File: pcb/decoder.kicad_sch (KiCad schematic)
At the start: 77 parts, among them J1 Conn_01x03_Socket, J2 Conn_01x03_Socket, J3 Conn_01x02_Socket, J4 Conn_01x02_Socket, J5 Conn_01x02_Socket, J6 Conn_01x02_Socket, J7 Conn_01x02_Socket, J8 Conn_01x03_Socket, Q1 IRLZ44N, Q10 BC817, Q11 FQP27P06, Q12 BC817, Q13 FQP27P06, Q15 BC817, Q2 FQP27P06, Q3 FQP27P06, Q4 IRLZ44N, Q5 BC817, Q6 BC817, Q7 FQP27P06, Q8 BC817, Q9 FQP27P06, U1 LM7805, U3 6N137

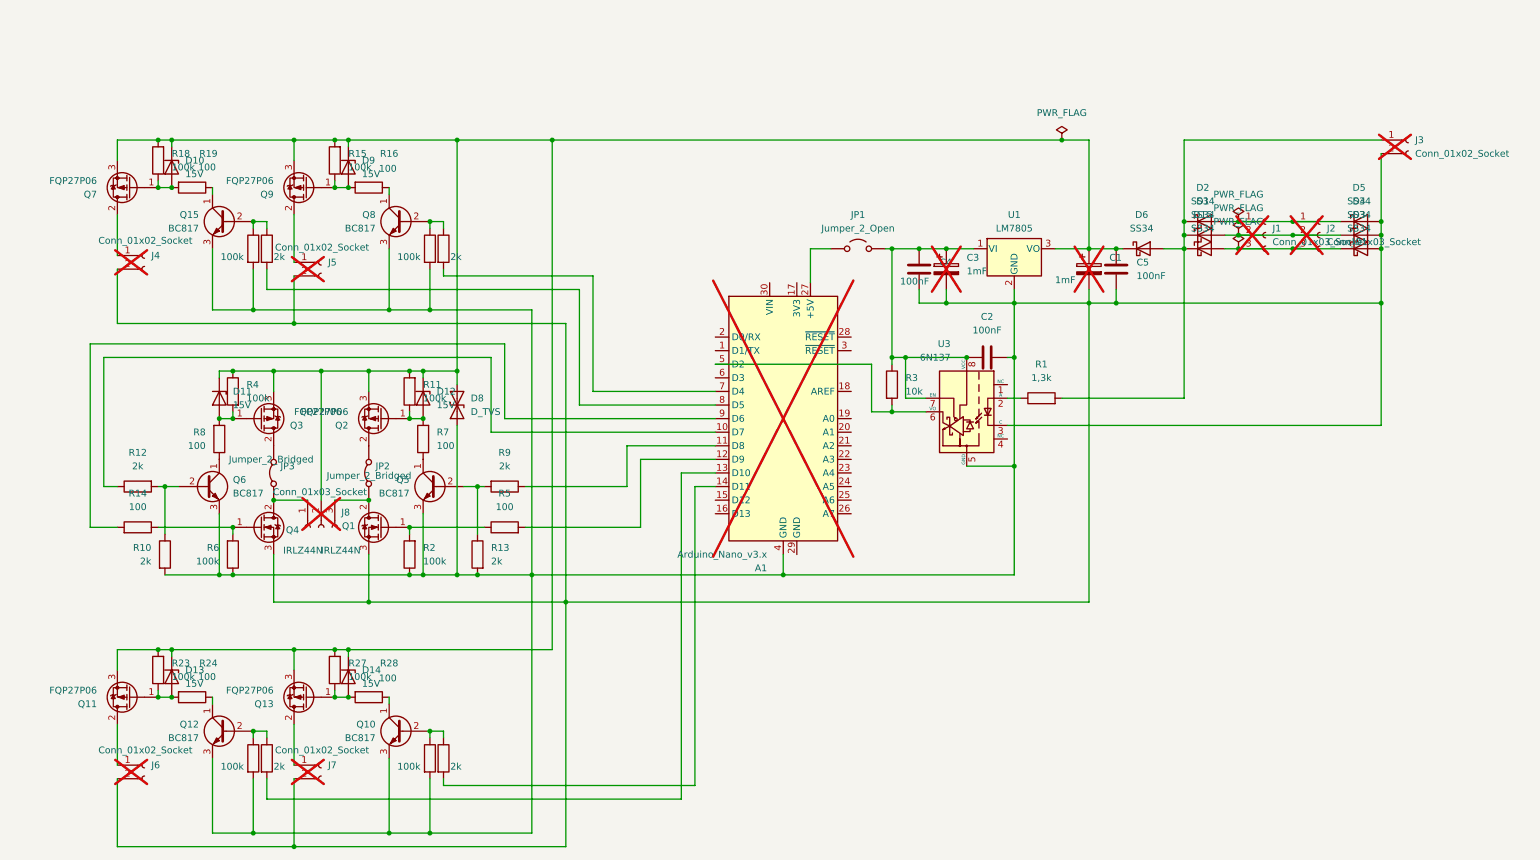
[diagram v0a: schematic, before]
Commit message: make PCB smaller
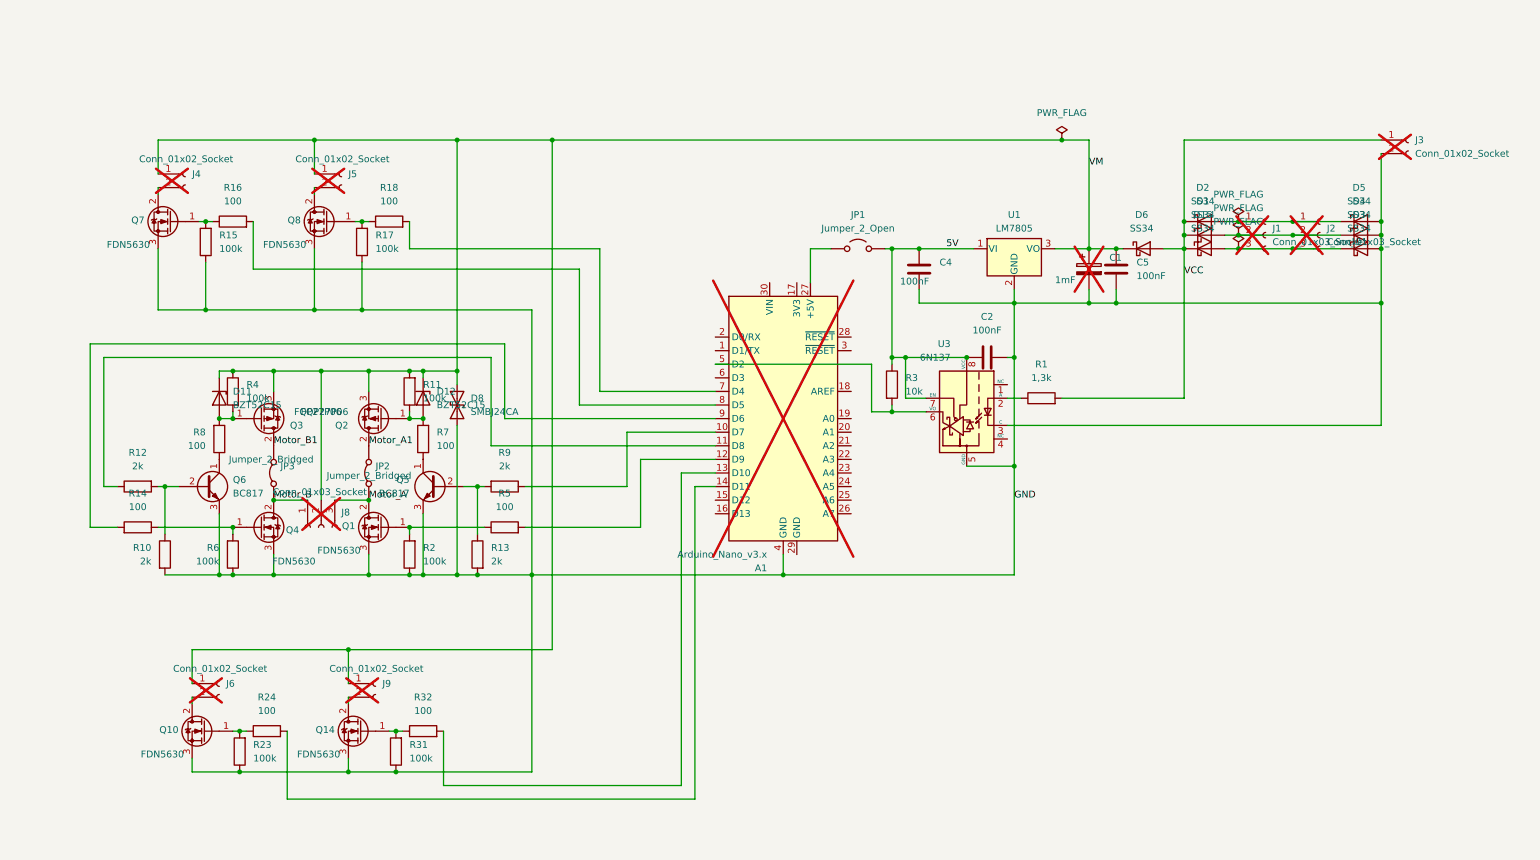
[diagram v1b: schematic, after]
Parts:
- removed C3: 1mF, Capacitor_THT:CP_Radial_D8.0mm_P3.50mm, symbol Device:C_Polarized
- removed D10, D13, D14, D9: 15V, Diode_SMD:D_SOD-523, symbol Device:D_Zener
- removed J7: Conn_01x02_Socket, Connector_PinHeader_2.54mm:PinHeader_1x02_P2.54mm_Vertical, symbol Connector:Conn_01x02_Socket
- removed Q10, Q12, Q15, Q8: BC817, Package_TO_SOT_SMD:SOT-23, symbol Transistor_BJT:BC547
- removed Q11, Q13, Q7, Q9: FQP27P06, Package_TO_SOT_SMD:TO-252-3_TabPin2, symbol Transistor_FET:FQP27P06
- removed R19, R28: 100, Capacitor_SMD:C_0201_0603Metric, symbol Device:R
- removed R20, R22, R26, R30: 2k, Capacitor_SMD:C_0201_0603Metric, symbol Device:R
- removed R21, R25, R27, R29: 100k, Capacitor_SMD:C_0201_0603Metric, symbol Device:R
- added J9: Conn_01x02_Socket, Connector_PinHeader_2.54mm:PinHeader_1x02_P2.54mm_Vertical, symbol Connector:Conn_01x02_Socket
- added Q10, Q14, Q7, Q8: FDN5630, Package_TO_SOT_SMD:SOT-23, symbol Transistor_FET:IRLZ44N
- added R31: 100k, Capacitor_SMD:C_0201_0603Metric, symbol Device:R
- added R32: 100, Capacitor_SMD:C_0201_0603Metric, symbol Device:R
- C1: footprint Capacitor_THT:CP_Radial_D12.5mm_P5.00mm -> Connector_PinHeader_2.54mm:PinHeader_1x02_P2.54mm_Vertical
- C2, C4, C5: LCSC C29936 -> (none)
- D1, D15, D2, D3, D4, D5, D6: LCSC C8678 -> (none)
- D11, D12: value 15V -> BZT52C15; LCSC C571376 -> (none)
- D8: value D_TVS -> SMBJ24CA; LCSC C151919 -> (none)
- Q1, Q4: value IRLZ44N -> FDN5630
- R1: LCSC C17384 -> (none)
- R10, R12, R13, R9: LCSC C17604 -> (none)
- R11, R15, R17, R2, R23, R4, R6: LCSC C149504 -> (none)
- R14, R16, R24, R5, R7, R8: LCSC C17408 -> (none)
- R18: value 100k -> 100; LCSC C149504 -> (none)
- R3: LCSC 17414 -> (none)
- U1: LCSC C6187 -> (none)
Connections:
- net VM: now reaches C1.1, C5.2, D11.1 (K), D12.1 (K), D6.1 (K), D8.2 (A2), J8.2 (Pin_2), Q2.3 (S), Q3.3 (S), R11.2, R4.1, U1.3 (VO)
- net VM: now also J4.1 (Pin_1), J5.1 (Pin_1), J6.1 (Pin_1), J9.1 (Pin_1); no longer R15.2, R18.2, R23.2
- net at R24.2: now also A1.14 (D11); no longer R23.1
- net GND: now reaches R17.1
- net GND: now also A1.4 (GND), C1.2, C2.2, C4.1, C5.1, D3.2 (A), D4.2 (A), D5.2 (A), D8.1 (A1), J3.2 (Pin_2), Q1.3 (S), Q4.3 (S), Q5.3 (E), Q6.3 (E), R10.2, R13.2, R15.1, R2.1, R23.1, R6.1, U1.2 (GND), U3.3 (C), U3.5 (GND), Q10.3 (S), Q14.3 (S), Q7.3 (S), Q8.3 (S), R31.1
- net at A1.7 (D4): now also R18.2
- net Motor_B: now reaches J8.1 (Pin_1), JP3.1 (A), Q4.2 (D)
- net Motor_B1: now reaches JP3.2 (B), Q3.2 (D)
- net at R24.1: now also R23.2, Q10.1 (G)
- net at R16.1: now also R15.2, Q7.1 (G)
- net at R16.2: now also A1.8 (D5); no longer R15.1
- net Motor_A: now reaches J8.3 (Pin_3), JP2.1 (A), Q1.2 (D)
- net Motor_A1: now reaches JP2.2 (B), Q2.2 (D)
- net at R18.1: now also R17.2, Q8.1 (G)
- net at R9.1: now also A1.10 (D7); no longer A1.11 (D8)
- net at A1.13 (D10): now also R32.2
- net 5V: now reaches C2.1, C4.2, JP1.2 (B), R3.1, U1.1 (VI), U3.7 (EN), U3.8 (VCC)
- net VCC: now reaches D1.1 (K), D15.1 (K), D2.1 (K), D6.2 (A), J3.1 (Pin_1), R1.2
- net at R12.1: now also A1.11 (D8); no longer A1.10 (D7)
- new net: Q14.1 (G), R31.2, R32.1
- new net: J9.2 (Pin_2), Q14.2 (D)
- new net: J5.2 (Pin_2), Q8.2 (D)
- new net: J6.2 (Pin_2), Q10.2 (D)
- new net: J4.2 (Pin_2), Q7.2 (D)

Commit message: fix some pcb part numbers
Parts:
- C2, C4, C5: LCSC (none) -> C29936
- D1, D15, D2, D3, D4, D5, D6: LCSC (none) -> C8678
- D11, D12: value BZT52C15 -> BZT585B15T-7; LCSC (none) -> C571376
- D8: value SMBJ24CA -> SMAJ24CA; LCSC (none) -> C151919
- JP1, JP2, JP3, U3: now not fitted; now left out of the parts list
- Q2, Q3: value FQP27P06 -> ROHM RD3L08BBJHRBTL; now not fitted; now left out of the parts list
- R1: LCSC (none) -> C17384
- R10, R12, R13, R9: LCSC (none) -> C17604
- R11, R15, R17, R2, R23, R31, R4, R6: LCSC (none) -> C149504
- R14, R16, R18, R24, R32, R5, R7, R8: LCSC (none) -> C17408
- R3: LCSC (none) -> 17414
- U1: LCSC (none) -> C6187

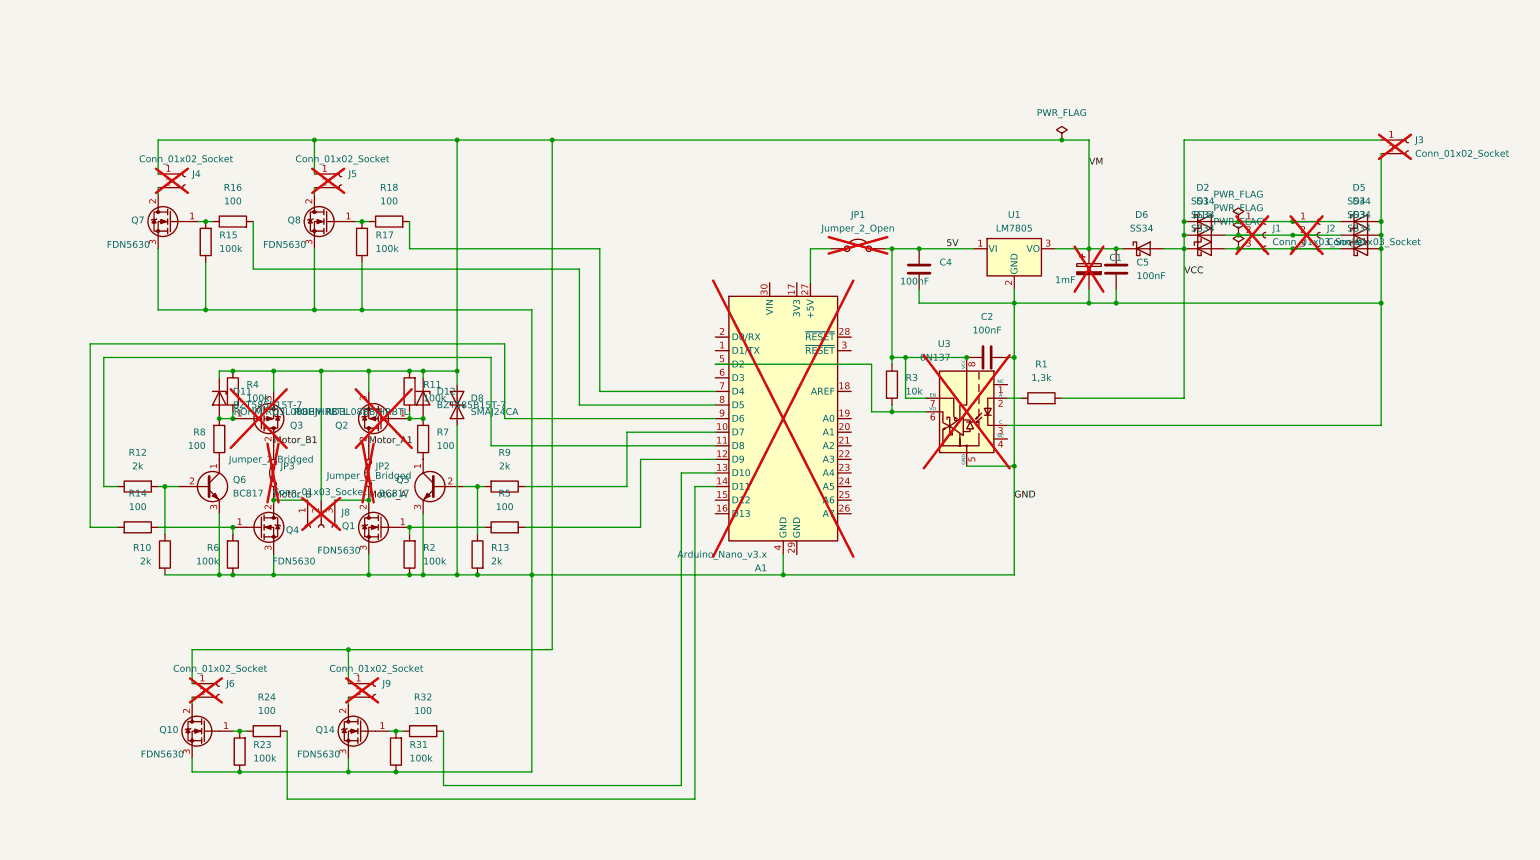
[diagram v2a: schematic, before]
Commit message: add tests
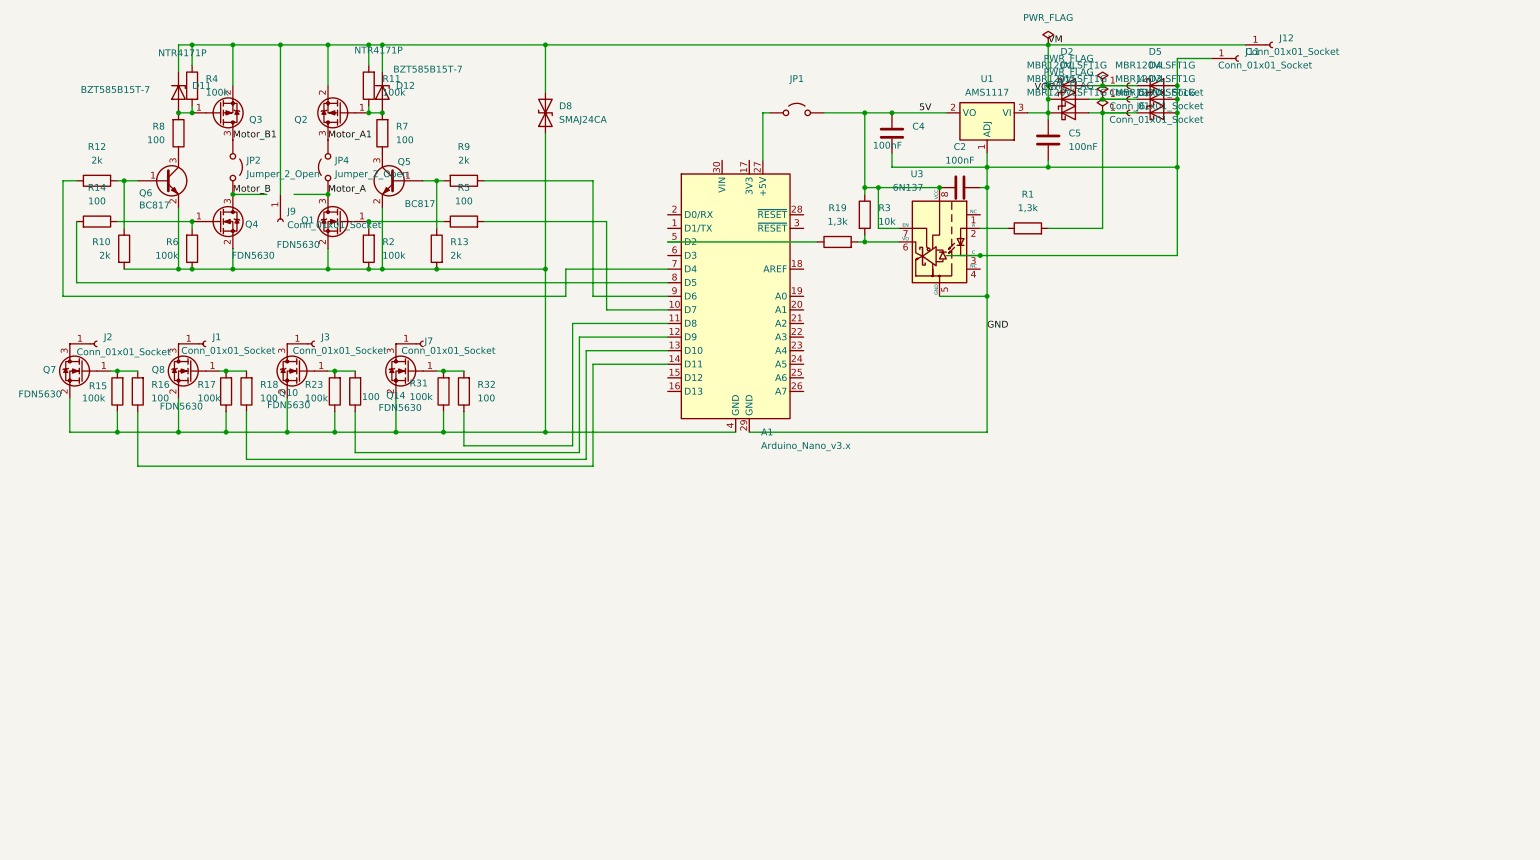
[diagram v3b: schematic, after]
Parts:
- removed C1: 1mF, Connector_PinHeader_2.54mm:PinHeader_1x02_P2.54mm_Vertical, symbol Device:C_Polarized
- removed D6: SS34, Diode_SMD:D_SMA, symbol Diode:SS34
- removed J1, J2, J8: Conn_01x03_Socket, Connector_PinHeader_2.54mm:PinHeader_1x03_P2.54mm_Vertical, symbol Connector:Conn_01x03_Socket
- removed J3, J4, J5, J6, J9: Conn_01x02_Socket, Connector_PinHeader_2.54mm:PinHeader_1x02_P2.54mm_Vertical, symbol Connector:Conn_01x02_Socket
- removed JP2, JP3: Jumper_2_Bridged, Jumper:SolderJumper-2_P1.3mm_Bridged_Pad1.0x1.5mm, symbol Jumper:Jumper_2_Bridged
- added J1, J11, J12, J2, J3, J4, J5, J6, J7, J9: Conn_01x01_Socket, TestPoint:TestPoint_Pad_1.0x1.0mm, symbol Connector:Conn_01x01_Socket
- added JP2, JP4: Jumper_2_Open, Jumper:SolderJumper-2_P1.3mm_Open_Pad1.0x1.5mm, symbol Jumper:Jumper_2_Open
- added R19: 1,3k, Capacitor_SMD:C_0201_0603Metric, symbol Device:R
- A1, JP1, U3: now fitted; now in the parts list
- D1, D15, D2, D3, D4, D5: value SS34 -> MBR120VLSFT1G; footprint Diode_SMD:D_SMA -> Diode_SMD:D_SOD-123
- Q1, Q10, Q14, Q4, Q7, Q8: symbol Transistor_FET:IRLZ44N -> Transistor_FET:2N7002
- Q2, Q3: value ROHM RD3L08BBJHRBTL -> NTR4171P; footprint Package_TO_SOT_SMD:TO-252-3_TabPin2 -> Package_TO_SOT_SMD:SOT-23; symbol Transistor_FET:FQP27P06 -> Transistor_FET:AO3401A; now fitted; now in the parts list
- Q5, Q6: symbol Transistor_BJT:BC547 -> Transistor_BJT:BC817
- U1: value LM7805 -> AMS1117; symbol Regulator_Linear:LM7805_TO220 -> Regulator_Linear:AMS1117
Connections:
- net 5V: now also U1.2 (VO); no longer U1.1 (VI)
- net GND: now also A1.29 (GND), U1.1 (ADJ), J11.1 (Pin_1); no longer A1.4 (GND), D8.1 (A1), Q1.3 (S), Q10.3 (S), Q14.3 (S), Q4.3 (S), Q5.3 (E), Q6.3 (E), Q7.3 (S), Q8.3 (S), R10.2, R13.2, R15.1, R17.1, R2.1, R23.1, R31.1, R6.1, U1.2 (GND)
- net Motor_A: now also Q1.3 (D), JP4.1 (A); no longer Q1.2 (D)
- net Motor_A1: now also Q2.3 (D), JP4.2 (B); no longer Q2.2 (D)
- net Motor_B: now also Q4.3 (D), JP2.2 (B); no longer Q4.2 (D)
- net Motor_B1: now also Q3.3 (D), JP2.1 (A); no longer Q3.2 (D)
- net VCC: no longer D1.1 (K), D15.1 (K), D2.1 (K), R1.2
- net VM: now also D1.1 (K), D15.1 (K), D2.1 (K), Q2.2 (S), Q3.2 (S), J12.1 (Pin_1), J9.1 (Pin_1); no longer Q2.3 (S), Q3.3 (S)
- net at Q14.1 (G), R31.2: now also R32.2; no longer R32.1
- net at Q14.2 (S): now also A1.4 (GND), D8.1 (A1), Q1.2 (S), Q10.2 (S), Q4.2 (S), Q5.2 (E), Q6.2 (E), Q7.2 (S), Q8.2 (S), R10.2, R13.2, R15.1, R17.1, R2.1, R23.1, R31.1, R6.1
- net at Q8.1 (G), R17.2: now also R18.2; no longer R18.1
- net at R10.1, R12.2: now also Q6.1 (B); no longer Q6.2 (B)
- net at R9.1: now also A1.9 (D6); no longer A1.10 (D7)
- net at R13.1, R9.2: now also Q5.1 (B); no longer Q5.2 (B)
- net at Q10.1 (G), R23.2: now also R24.2; no longer R24.1
- net at R3.2, U3.6 (VO): now also R19.2; no longer A1.5 (D2)
- net at A1.7 (D4): now also R12.1; no longer R18.2
- net at D2.2 (A), D5.1 (K): now also J4.1 (Pin_1)
- net at D1.2 (A), D4.1 (K): now also J5.1 (Pin_1)
- net at D15.2 (A), D3.1 (K): now also R1.2, J6.1 (Pin_1)
- net at A1.11 (D8): now also R32.1; no longer R12.1
- net at A1.13 (D10): now also R18.1; no longer R32.2
- net at R7.1: now also Q5.3 (C); no longer Q5.1 (C)
- net at Q7.1 (G), R15.2: now also R16.2; no longer R16.1
- net at A1.8 (D5): now also R14.2; no longer R16.2
- net at A1.14 (D11): now also R16.1; no longer R24.2
- net at A1.12 (D9): now also R24.1; no longer R5.2
- net at R8.1: now also Q6.3 (C); no longer Q6.1 (C)
- new net: J7.1 (Pin_1), Q14.3 (D)
- new net: J1.1 (Pin_1), Q8.3 (D)
- new net: A1.5 (D2), R19.1
- new net: J2.1 (Pin_1), Q7.3 (D)
- new net: A1.10 (D7), R5.2
- new net: J3.1 (Pin_1), Q10.3 (D)
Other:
- moved on the sheet: C2, C4, C5, D1, D11, D12, D15, D2, D3, D4, D5, D8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
